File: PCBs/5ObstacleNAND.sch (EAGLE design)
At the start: 4 parts, among them IC1 74ALS00N, IC2 74LS32N

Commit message: updated something
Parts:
- added IC3: 7805DT, adafruit:7805DT
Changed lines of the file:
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@@
 <layer number="56" name="wert" color="7" fill="1" visible="no" active="no"/>
 <layer number="57" name="tCAD" color="7" fill="1" visible="no" active="no"/>
+<layer number="59" name="tCarbon" color="7" fill="1" visible="no" active="no"/>
+<layer number="60" name="bCarbon" color="7" fill="1" visible="no" active="no"/>
 <layer number="88" name="SimResults" color="9" fill="1" visible="yes" active="yes"/>
 <layer number="89" name="SimProbes" color="9" fill="1" visible="yes" active="yes"/>
@@
 <layer number="113" name="IDFDebug" color="4" fill="1" visible="yes" active="yes"/>
 <layer number="116" name="Patch_BOT" color="9" fill="4" visible="yes" active="yes"/>
+<layer number="118" name="Rect_Pads" color="7" fill="1" visible="no" active="no"/>
 <layer number="121" name="_tsilk" color="7" fill="1" visible="yes" active="yes"/>
 <layer number="122" name="_bsilk" color="7" fill="1" visible="yes" active="yes"/>
@@
 <layer number="127" name="_tValues" color="7" fill="1" visible="yes" active="yes"/>
 <layer number="128" name="_bValues" color="7" fill="1" visible="yes" active="yes"/>
+<layer number="129" name="Mask" color="7" fill="1" visible="yes" active="yes"/>
 <layer number="131" name="tAdjust" color="7" fill="1" visible="yes" active="yes"/>
 <layer number="132" name="bAdjust" color="7" fill="1" visible="yes" active="yes"/>
@@
 <layer number="230" name="230bmp" color="7" fill="1" visible="yes" active="yes"/>
 <layer number="231" name="231bmp" color="7" fill="1" visible="yes" active="yes"/>
+<layer number="232" name="Eagle3D_PG2" color="7" fill="1" visible="no" active="no"/>
+<layer number="233" name="Eagle3D_PG3" color="7" fill="1" visible="no" active="no"/>
 <layer number="248" name="Housing" color="7" fill="1" visible="yes" active="yes"/>
 <layer number="249" name="Edge" color="7" fill="1" visible="yes" active="yes"/>
@@
 <layer number="251" name="SMDround" color="12" fill="11" visible="no" active="no"/>
 <layer number="254" name="cooling" color="7" fill="1" visible="yes" active="yes"/>
+<layer number="255" name="routoute" color="7" fill="1" visible="yes" active="yes"/>
 </layers>
 <schematic xreflabel="%F%N/%S.%C%R" xrefpart="/%S.%C%R">
@@
 <part name="OUTPUT" library="Rembrandt Electronics - JST XH Connectors v1-0" deviceset="JST-XH-02-PIN" device="-LONG-PAD"/>
 <part name="SUPPLY4" library="supply2" library_urn="urn:adsk.eagle:library:372" deviceset="GND" device=""/>
+<part name="IC3" library="adafruit" deviceset="78*" device="DT" technology="05"/>
 </parts>
 <sheets>
@@
 <attribute name="VALUE" x="140.335" y="57.785" size="1.778" layer="96"/>
 </instance>
+<instance part="IC3" gate="A1" x="-7.62" y="109.22" smashed="yes">
+<attribute name="NAME" x="-15.24" y="114.935" size="1.778" layer="95"/>
+<attribute name="VALUE" x="-15.24" y="112.395" size="1.778" layer="96"/>
+</instance>
 </instances>

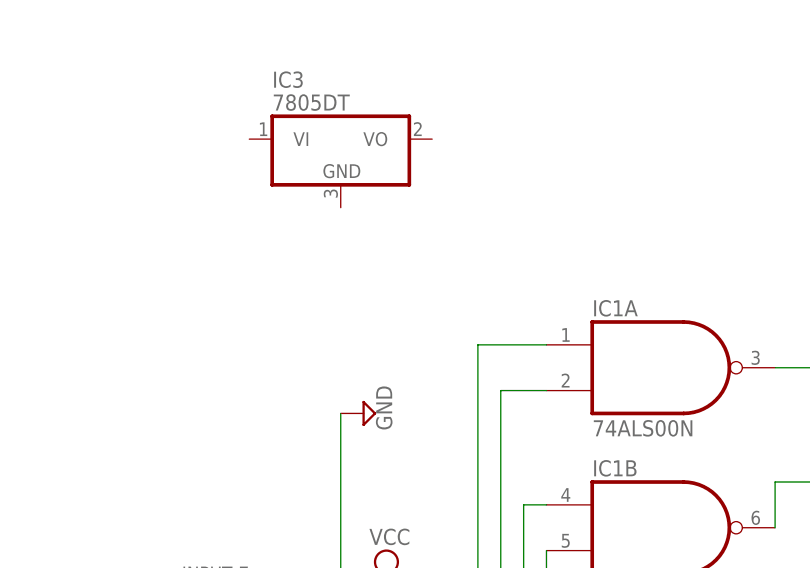
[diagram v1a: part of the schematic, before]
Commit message: Nand Gate Board updated
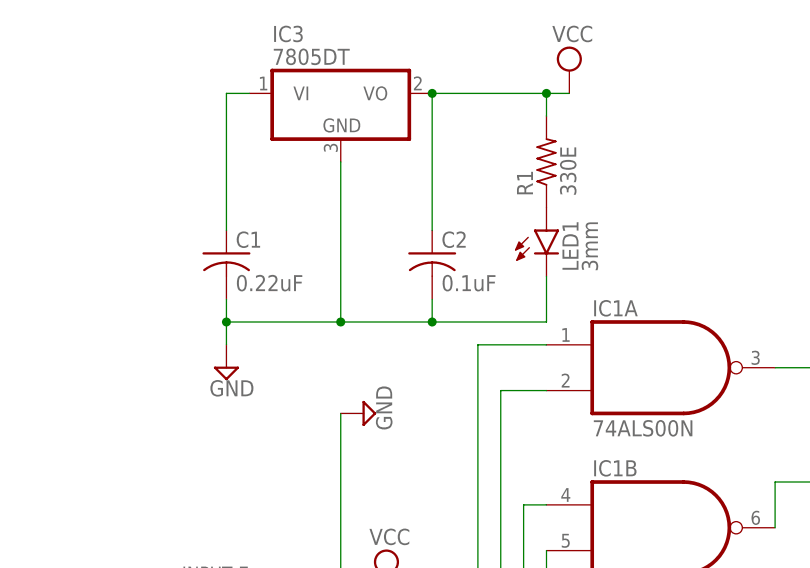
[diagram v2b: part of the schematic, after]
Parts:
- added C1: 0.22uF, adafruit:C-USC0805
- added C2: 0.1uF, adafruit:C-USC0805
- added LED1: 3mm, led:LEDSML0805
- added R1: 330E, rcl:R-US_R0805
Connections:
- new net N$12: LED1.A, R1.1
- new net N$13: C1.1, IC3.VI
- net GND: now also C1.2, C2.2, IC3.GND, LED1.C
- net VCC: now also C2.1, IC3.VO, R1.2
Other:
- moved on the sheet: IC3
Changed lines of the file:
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@@
 <part name="SUPPLY4" library="supply2" library_urn="urn:adsk.eagle:library:372" deviceset="GND" device=""/>
 <part name="IC3" library="adafruit" deviceset="78*" device="DT" technology="05"/>
+<part name="C1" library="adafruit" deviceset="C-US" device="C0805" value="0.22uF"/>
+<part name="C2" library="adafruit" deviceset="C-US" device="C0805" value="0.1uF"/>
+<part name="LED1" library="led" library_urn="urn:adsk.eagle:library:259" deviceset="LED" device="SML0805" package3d_urn="urn:adsk.eagle:package:15830/1" value="3mm"/>
+<part name="R1" library="rcl" library_urn="urn:adsk.eagle:library:334" deviceset="R-US_" device="R0805" package3d_urn="urn:adsk.eagle:package:23553/2" value="330E"/>
+<part name="SUPPLY5" library="supply2" library_urn="urn:adsk.eagle:library:372" deviceset="GND" device=""/>
+<part name="SUPPLY6" library="supply2" library_urn="urn:adsk.eagle:library:372" deviceset="VCC" device=""/>
 </parts>
 <sheets>
@@
 <attribute name="VALUE" x="140.335" y="57.785" size="1.778" layer="96"/>
 </instance>
-<instance part="IC3" gate="A1" x="-7.62" y="109.22" smashed="yes">
-<attribute name="NAME" x="-15.24" y="114.935" size="1.778" layer="95"/>
-<attribute name="VALUE" x="-15.24" y="112.395" size="1.778" layer="96"/>
+<instance part="IC3" gate="A1" x="-7.62" y="114.3" smashed="yes">
+<attribute name="NAME" x="-15.24" y="120.015" size="1.778" layer="95"/>
+<attribute name="VALUE" x="-15.24" y="117.475" size="1.778" layer="96"/>
+</instance>
+<instance part="C1" gate="G$1" x="-20.32" y="96.52" smashed="yes">
+<attribute name="NAME" x="-19.304" y="97.155" size="1.778" layer="95"/>
+<attribute name="VALUE" x="-19.304" y="92.329" size="1.778" layer="96"/>
+</instance>
+<instance part="C2" gate="G$1" x="2.54" y="96.52" smashed="yes">
+<attribute name="NAME" x="3.556" y="97.155" size="1.778" layer="95"/>
+<attribute name="VALUE" x="3.556" y="92.329" size="1.778" layer="96"/>
+</instance>
+<instance part="LED1" gate="G$1" x="15.24" y="99.06" smashed="yes">
+<attribute name="NAME" x="18.796" y="94.488" size="1.778" layer="95" rot="R90"/>
+<attribute name="VALUE" x="20.955" y="94.488" size="1.778" layer="96" rot="R90"/>
+</instance>
+<instance part="R1" gate="G$1" x="15.24" y="106.68" smashed="yes" rot="R90">
+<attribute name="NAME" x="13.7414" y="102.87" size="1.778" layer="95" rot="R90"/>
+<attribute name="VALUE" x="18.542" y="102.87" size="1.778" layer="96" rot="R90"/>
+</instance>
+<instance part="SUPPLY5" gate="GND" x="-20.32" y="83.82" smashed="yes">
+<attribute name="VALUE" x="-22.225" y="80.645" size="1.778" layer="96"/>
+</instance>
+<instance part="SUPPLY6" gate="G$1" x="17.78" y="116.84" smashed="yes">
+<attribute name="VALUE" x="15.875" y="120.015" size="1.778" layer="96"/>
 </instance>
 </instances>
@@
 <pinref part="SUPPLY4" gate="GND" pin="GND"/>
 </segment>
+<segment>
+<pinref part="C2" gate="G$1" pin="2"/>
+<wire x1="2.54" y1="91.44" x2="2.54" y2="88.9" width="0.1524" layer="91"/>
+<pinref part="C1" gate="G$1" pin="2"/>
+<wire x1="2.54" y1="88.9" x2="-7.62" y2="88.9" width="0.1524" layer="91"/>
+<wire x1="-7.62" y1="88.9" x2="-20.32" y2="88.9" width="0.1524" layer="91"/>
+<wire x1="-20.32" y1="88.9" x2="-20.32" y2="91.44" width="0.1524" layer="91"/>
+<pinref part="LED1" gate="G$1" pin="C"/>
+<wire x1="15.24" y1="93.98" x2="15.24" y2="88.9" width="0.1524" layer="91"/>
+<wire x1="15.24" y1="88.9" x2="2.54" y2="88.9" width="0.1524" layer="91"/>
+<pinref part="IC3" gate="A1" pin="GND"/>
+<wire x1="-7.62" y1="106.68" x2="-7.62" y2="88.9" width="0.1524" layer="91"/>
+<junction x="-7.62" y="88.9"/>
+<pinref part="SUPPLY5" gate="GND" pin="GND"/>
+<wire x1="-20.32" y1="86.36" x2="-20.32" y2="88.9" width="0.1524" layer="91"/>
+<junction x="-20.32" y="88.9"/>
+<junction x="2.54" y="88.9"/>
+</segment>
 </net>
 <net name="VCC" class="0">
@@
 <pinref part="IC1" gate="C" pin="I1"/>
 <pinref part="SUPPLY3" gate="G$1" pin="VCC"/>
+</segment>
+<segment>
+<pinref part="SUPPLY6" gate="G$1" pin="VCC"/>
+<pinref part="IC3" gate="A1" pin="VO"/>
+<pinref part="C2" gate="G$1" pin="1"/>
+<wire x1="2.54" y1="114.3" x2="2.54" y2="99.06" width="0.1524" layer="91"/>
+<wire x1="2.54" y1="114.3" x2="15.24" y2="114.3" width="0.1524" layer="91"/>
+<junction x="2.54" y="114.3"/>
+<pinref part="R1" gate="G$1" pin="2"/>
+<wire x1="15.24" y1="114.3" x2="15.24" y2="111.76" width="0.1524" layer="91"/>
+<wire x1="17.78" y1="114.3" x2="15.24" y2="114.3" width="0.1524" layer="91"/>
+<junction x="15.24" y="114.3"/>
 </segment>
 </net>
@@
 <pinref part="OUTPUT" gate="-1" pin="S"/>
 <wire x1="132.08" y1="66.04" x2="142.24" y2="66.04" width="0.1524" layer="91"/>
+</segment>
+</net>
+<net name="N$12" class="0">
+<segment>
+<pinref part="LED1" gate="G$1" pin="A"/>
+<pinref part="R1" gate="G$1" pin="1"/>
+</segment>
+</net>
+<net name="N$13" class="0">
+<segment>
+<pinref part="C1" gate="G$1" pin="1"/>
+<wire x1="-20.32" y1="99.06" x2="-20.32" y2="114.3" width="0.1524" layer="91"/>
+<pinref part="IC3" gate="A1" pin="VI"/>
+<wire x1="-20.32" y1="114.3" x2="-17.78" y2="114.3" width="0.1524" layer="91"/>
 </segment>
 </net>
@@
 packages will not be understood (or retained) with this version.
 </note>
+<note version="8.4" severity="warning">
+Since Version 8.4, EAGLE supports properties for SPICE simulation.
+Probes in schematics and SPICE mapping objects found in parts and library devices
+will not be understood with this version. Update EAGLE to the latest version
+for full support of SPICE simulation.
+</note>
 </compatibility>

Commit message: added connector for Vin and 5V
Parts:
- added 5V, OUTPUT2: JST-XH-02-PIN-LONG-PAD, Rembrandt Electronics - JST XH Connectors v1-0:JST-XH-02-PIN-LONG-PAD
- added VIN(7V-9V): (no value), con-wago-500:W237-102
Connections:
- net GND: now also 5V-2.S, OUTPUT2-2.S, VIN(7V-9V)-2.KL
- net N$13: now also VIN(7V-9V)-1.KL
- net VCC: now also OUTPUT2-1.S
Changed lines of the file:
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@@
 <part name="SUPPLY5" library="supply2" library_urn="urn:adsk.eagle:library:372" deviceset="GND" device=""/>
 <part name="SUPPLY6" library="supply2" library_urn="urn:adsk.eagle:library:372" deviceset="VCC" device=""/>
+<part name="VIN(7V-9V)" library="con-wago-500" library_urn="urn:adsk.eagle:library:195" deviceset="W237-102" device="" package3d_urn="urn:adsk.eagle:package:10688/1"/>
+<part name="5V" library="Rembrandt Electronics - JST XH Connectors v1-0" deviceset="JST-XH-02-PIN" device="-LONG-PAD"/>
+<part name="OUTPUT2" library="Rembrandt Electronics - JST XH Connectors v1-0" deviceset="JST-XH-02-PIN" device="-LONG-PAD"/>
 </parts>
 <sheets>
@@
 <attribute name="VALUE" x="15.875" y="120.015" size="1.778" layer="96"/>
 </instance>
+<instance part="VIN(7V-9V)" gate="-1" x="-35.56" y="114.3" smashed="yes">
+<attribute name="NAME" x="-35.56" y="115.189" size="1.778" layer="95" rot="R180"/>
+</instance>
+<instance part="VIN(7V-9V)" gate="-2" x="-35.56" y="109.22" smashed="yes">
+<attribute name="VALUE" x="-38.1" y="105.537" size="1.778" layer="96"/>
+<attribute name="NAME" x="-35.56" y="110.109" size="1.778" layer="95" rot="R180"/>
+</instance>
+<instance part="5V" gate="-2" x="30.48" y="111.76" smashed="yes">
+<attribute name="NAME" x="33.02" y="110.998" size="1.524" layer="95"/>
+</instance>
+<instance part="5V" gate="-1" x="33.02" y="114.3" smashed="yes">
+<attribute name="NAME" x="35.56" y="113.538" size="1.524" layer="95"/>
+<attribute name="VALUE" x="32.258" y="115.697" size="1.778" layer="96"/>
+</instance>
+<instance part="OUTPUT2" gate="-2" x="30.48" y="111.76" smashed="yes">
+<attribute name="NAME" x="33.02" y="110.998" size="1.524" layer="95"/>
+</instance>
+<instance part="OUTPUT2" gate="-1" x="30.48" y="114.3" smashed="yes">
+<attribute name="NAME" x="33.02" y="113.538" size="1.524" layer="95"/>
+<attribute name="VALUE" x="29.718" y="115.697" size="1.778" layer="96"/>
+</instance>
 </instances>
 <busses>
@@
 <wire x1="-20.32" y1="88.9" x2="-20.32" y2="91.44" width="0.1524" layer="91"/>
 <pinref part="LED1" gate="G$1" pin="C"/>
-<wire x1="15.24" y1="93.98" x2="15.24" y2="88.9" width="0.1524" layer="91"/>
+<wire x1="15.24" y1="93.98" x2="15.24" y2="91.44" width="0.1524" layer="91"/>
+<wire x1="15.24" y1="91.44" x2="15.24" y2="88.9" width="0.1524" layer="91"/>
 <wire x1="15.24" y1="88.9" x2="2.54" y2="88.9" width="0.1524" layer="91"/>
 <pinref part="IC3" gate="A1" pin="GND"/>
@@
 <junction x="-20.32" y="88.9"/>
 <junction x="2.54" y="88.9"/>
+<pinref part="VIN(7V-9V)" gate="-2" pin="KL"/>
+<wire x1="-30.48" y1="109.22" x2="-30.48" y2="88.9" width="0.1524" layer="91"/>
+<wire x1="-30.48" y1="88.9" x2="-20.32" y2="88.9" width="0.1524" layer="91"/>
+<pinref part="5V" gate="-2" pin="S"/>
+<pinref part="OUTPUT2" gate="-2" pin="S"/>
+<wire x1="27.94" y1="111.76" x2="27.94" y2="91.44" width="0.1524" layer="91"/>
+<wire x1="27.94" y1="91.44" x2="15.24" y2="91.44" width="0.1524" layer="91"/>
+<junction x="27.94" y="111.76"/>
+<junction x="15.24" y="91.44"/>
 </segment>
 </net>
@@
 <wire x1="17.78" y1="114.3" x2="15.24" y2="114.3" width="0.1524" layer="91"/>
 <junction x="15.24" y="114.3"/>
+<pinref part="OUTPUT2" gate="-1" pin="S"/>
+<wire x1="17.78" y1="114.3" x2="27.94" y2="114.3" width="0.1524" layer="91"/>
+<junction x="17.78" y="114.3"/>
 </segment>
 </net>
@@
 <pinref part="IC3" gate="A1" pin="VI"/>
 <wire x1="-20.32" y1="114.3" x2="-17.78" y2="114.3" width="0.1524" layer="91"/>
-</segment>
-</net>
+<pinref part="VIN(7V-9V)" gate="-1" pin="KL"/>
+<wire x1="-20.32" y1="114.3" x2="-30.48" y2="114.3" width="0.1524" layer="91"/>
+<junction x="-20.32" y="114.3"/>
+</segment>
+</net>

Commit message: updated nand gate amd nodmcu
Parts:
- removed OUTPUT2: JST-XH-02-PIN-LONG-PAD, Rembrandt Electronics - JST XH Connectors v1-0:JST-XH-02-PIN-LONG-PAD
- VIN: value (none) -> 7V-9v
- renumbered VIN(7V-9V) to VIN
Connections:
- net GND: no longer OUTPUT2-2.S
- net VCC: now also 5V-1.S; no longer OUTPUT2-1.S
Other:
- moved on the sheet: 5V-1
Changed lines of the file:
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@@
 <part name="SUPPLY5" library="supply2" library_urn="urn:adsk.eagle:library:372" deviceset="GND" device=""/>
 <part name="SUPPLY6" library="supply2" library_urn="urn:adsk.eagle:library:372" deviceset="VCC" device=""/>
-<part name="VIN(7V-9V)" library="con-wago-500" library_urn="urn:adsk.eagle:library:195" deviceset="W237-102" device="" package3d_urn="urn:adsk.eagle:package:10688/1"/>
+<part name="VIN" library="con-wago-500" library_urn="urn:adsk.eagle:library:195" deviceset="W237-102" device="" package3d_urn="urn:adsk.eagle:package:10688/1" value="7V-9v"/>
 <part name="5V" library="Rembrandt Electronics - JST XH Connectors v1-0" deviceset="JST-XH-02-PIN" device="-LONG-PAD"/>
-<part name="OUTPUT2" library="Rembrandt Electronics - JST XH Connectors v1-0" deviceset="JST-XH-02-PIN" device="-LONG-PAD"/>
 </parts>
 <sheets>
@@
 <attribute name="VALUE" x="15.875" y="120.015" size="1.778" layer="96"/>
 </instance>
-<instance part="VIN(7V-9V)" gate="-1" x="-35.56" y="114.3" smashed="yes">
+<instance part="VIN" gate="-1" x="-35.56" y="114.3" smashed="yes">
 <attribute name="NAME" x="-35.56" y="115.189" size="1.778" layer="95" rot="R180"/>
 </instance>
-<instance part="VIN(7V-9V)" gate="-2" x="-35.56" y="109.22" smashed="yes">
+<instance part="VIN" gate="-2" x="-35.56" y="109.22" smashed="yes">
 <attribute name="VALUE" x="-38.1" y="105.537" size="1.778" layer="96"/>
 <attribute name="NAME" x="-35.56" y="110.109" size="1.778" layer="95" rot="R180"/>
@@
 <attribute name="NAME" x="33.02" y="110.998" size="1.524" layer="95"/>
 </instance>
-<instance part="5V" gate="-1" x="33.02" y="114.3" smashed="yes">
-<attribute name="NAME" x="35.56" y="113.538" size="1.524" layer="95"/>
-<attribute name="VALUE" x="32.258" y="115.697" size="1.778" layer="96"/>
-</instance>
-<instance part="OUTPUT2" gate="-2" x="30.48" y="111.76" smashed="yes">
-<attribute name="NAME" x="33.02" y="110.998" size="1.524" layer="95"/>
-</instance>
-<instance part="OUTPUT2" gate="-1" x="30.48" y="114.3" smashed="yes">
+<instance part="5V" gate="-1" x="30.48" y="114.3" smashed="yes">
 <attribute name="NAME" x="33.02" y="113.538" size="1.524" layer="95"/>
 <attribute name="VALUE" x="29.718" y="115.697" size="1.778" layer="96"/>
@@
 <junction x="-20.32" y="88.9"/>
 <junction x="2.54" y="88.9"/>
-<pinref part="VIN(7V-9V)" gate="-2" pin="KL"/>
+<pinref part="VIN" gate="-2" pin="KL"/>
 <wire x1="-30.48" y1="109.22" x2="-30.48" y2="88.9" width="0.1524" layer="91"/>
 <wire x1="-30.48" y1="88.9" x2="-20.32" y2="88.9" width="0.1524" layer="91"/>
-<pinref part="5V" gate="-2" pin="S"/>
-<pinref part="OUTPUT2" gate="-2" pin="S"/>
 <wire x1="27.94" y1="111.76" x2="27.94" y2="91.44" width="0.1524" layer="91"/>
 <wire x1="27.94" y1="91.44" x2="15.24" y2="91.44" width="0.1524" layer="91"/>
-<junction x="27.94" y="111.76"/>
 <junction x="15.24" y="91.44"/>
+<pinref part="5V" gate="-2" pin="S"/>
 </segment>
 </net>
@@
 <wire x1="17.78" y1="114.3" x2="15.24" y2="114.3" width="0.1524" layer="91"/>
 <junction x="15.24" y="114.3"/>
-<pinref part="OUTPUT2" gate="-1" pin="S"/>
 <wire x1="17.78" y1="114.3" x2="27.94" y2="114.3" width="0.1524" layer="91"/>
 <junction x="17.78" y="114.3"/>
+<pinref part="5V" gate="-1" pin="S"/>
 </segment>
 </net>
@@
 <pinref part="IC3" gate="A1" pin="VI"/>
 <wire x1="-20.32" y1="114.3" x2="-17.78" y2="114.3" width="0.1524" layer="91"/>
-<pinref part="VIN(7V-9V)" gate="-1" pin="KL"/>
+<pinref part="VIN" gate="-1" pin="KL"/>
 <wire x1="-20.32" y1="114.3" x2="-30.48" y2="114.3" width="0.1524" layer="91"/>
 <junction x="-20.32" y="114.3"/>

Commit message: updated
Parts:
- added LED2: Green, led:LEDSML0805
- added R2: 10K, rcl:R-US_R0805
- added R3: 330E, rcl:R-US_R0805
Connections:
- new net N$11: LED2.C, R3.1
- net GND: now also R2.1, R3.2
- net N$10: now also LED2.A, R2.2
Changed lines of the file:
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@@
 <part name="VIN" library="con-wago-500" library_urn="urn:adsk.eagle:library:195" deviceset="W237-102" device="" package3d_urn="urn:adsk.eagle:package:10688/1" value="7V-9v"/>
 <part name="5V" library="Rembrandt Electronics - JST XH Connectors v1-0" deviceset="JST-XH-02-PIN" device="-LONG-PAD"/>
+<part name="R2" library="rcl" library_urn="urn:adsk.eagle:library:334" deviceset="R-US_" device="R0805" package3d_urn="urn:adsk.eagle:package:23553/2" value="10K"/>
+<part name="SUPPLY7" library="supply2" library_urn="urn:adsk.eagle:library:372" deviceset="GND" device=""/>
+<part name="LED2" library="led" library_urn="urn:adsk.eagle:library:259" deviceset="LED" device="SML0805" package3d_urn="urn:adsk.eagle:package:15830/1" value="Green"/>
+<part name="R3" library="rcl" library_urn="urn:adsk.eagle:library:334" deviceset="R-US_" device="R0805" package3d_urn="urn:adsk.eagle:package:23553/2" value="330E"/>
+<part name="SUPPLY8" library="supply2" library_urn="urn:adsk.eagle:library:372" deviceset="GND" device=""/>
 </parts>
 <sheets>
@@
 <attribute name="NAME" x="33.02" y="113.538" size="1.524" layer="95"/>
 <attribute name="VALUE" x="29.718" y="115.697" size="1.778" layer="96"/>
+</instance>
+<instance part="R2" gate="G$1" x="134.62" y="60.96" smashed="yes" rot="R90">
+<attribute name="NAME" x="133.1214" y="57.15" size="1.778" layer="95" rot="R90"/>
+<attribute name="VALUE" x="137.922" y="57.15" size="1.778" layer="96" rot="R90"/>
+</instance>
+<instance part="SUPPLY7" gate="GND" x="134.62" y="53.34" smashed="yes">
+<attribute name="VALUE" x="132.715" y="50.165" size="1.778" layer="96"/>
+</instance>
+<instance part="LED2" gate="G$1" x="134.62" y="78.74" smashed="yes" rot="R180">
+<attribute name="NAME" x="131.064" y="83.312" size="1.778" layer="95" rot="R270"/>
+<attribute name="VALUE" x="128.905" y="83.312" size="1.778" layer="96" rot="R270"/>
+</instance>
+<instance part="R3" gate="G$1" x="134.62" y="88.9" smashed="yes" rot="R90">
+<attribute name="NAME" x="133.1214" y="85.09" size="1.778" layer="95" rot="R90"/>
+<attribute name="VALUE" x="137.922" y="85.09" size="1.778" layer="96" rot="R90"/>
+</instance>
+<instance part="SUPPLY8" gate="GND" x="134.62" y="96.52" smashed="yes" rot="R180">
+<attribute name="VALUE" x="136.525" y="99.695" size="1.778" layer="96" rot="R180"/>
 </instance>
 </instances>
@@
 <pinref part="5V" gate="-2" pin="S"/>
 </segment>
+<segment>
+<pinref part="R2" gate="G$1" pin="1"/>
+<pinref part="SUPPLY7" gate="GND" pin="GND"/>
+</segment>
+<segment>
+<pinref part="R3" gate="G$1" pin="2"/>
+<pinref part="SUPPLY8" gate="GND" pin="GND"/>
+</segment>
 </net>
 <net name="VCC" class="0">
@@
 <pinref part="IC2" gate="B" pin="O"/>
 <pinref part="OUTPUT" gate="-1" pin="S"/>
-<wire x1="132.08" y1="66.04" x2="142.24" y2="66.04" width="0.1524" layer="91"/>
+<wire x1="132.08" y1="66.04" x2="134.62" y2="66.04" width="0.1524" layer="91"/>
+<pinref part="R2" gate="G$1" pin="2"/>
+<wire x1="134.62" y1="66.04" x2="142.24" y2="66.04" width="0.1524" layer="91"/>
+<junction x="134.62" y="66.04"/>
+<pinref part="LED2" gate="G$1" pin="A"/>
+<wire x1="134.62" y1="76.2" x2="134.62" y2="66.04" width="0.1524" layer="91"/>
 </segment>
 </net>
@@
 </segment>
 </net>
+<net name="N$11" class="0">
+<segment>
+<pinref part="LED2" gate="G$1" pin="C"/>
+<pinref part="R3" gate="G$1" pin="1"/>
+</segment>
+</net>
